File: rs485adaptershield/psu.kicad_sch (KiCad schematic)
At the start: 3 parts

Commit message: more work
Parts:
- added C10: 1u, Capacitor_SMD:C_1210_3225Metric, symbol Device:C
- added C11: 10p, Capacitor_SMD:C_1210_3225Metric, symbol Device:C
- added C7, C8: 22u, Capacitor_SMD:C_1210_3225Metric, symbol Device:C
- added C9: 100n, Capacitor_SMD:C_1210_3225Metric, symbol Device:C
- added R17: 47k, Resistor_SMD:R_0805_2012Metric, symbol Device:R
- added R18: 10k, Resistor_SMD:R_0805_2012Metric, symbol Device:R
- added U5: TPSM33606S5QRDNRQ1, RDN0011A_TEX, symbol TPSM33606S5QRDNRQ1:TPSM33606S5QRDNRQ1
- C3: value 22u -> 4.7u
- R10: value 470 -> 560
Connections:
- net GND: now also C10.2, C7.2, C8.2, C9.2, R18.2, U5.10 (GND), U5.11 (MODE/SYNCH)
- net +12V renamed VIN
- net VIN: now also C9.1, U5.2 (EN), U5.3 (VIN)
- net +5V renamed VUSB
- net VUSB: now also C11.1, C7.1, C8.1, R17.1, U5.4 (VOUT)
- new net: C10.1, U5.8 (VCC)
- new net FB: C11.2, R17.2, R18.1, U5.9 (FB)
- no-connect marks 0 -> 4
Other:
- moved on the sheet: C3

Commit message: more progress
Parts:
- removed D4: LED, LED_SMD:LED_0805_2012Metric, symbol Device:LED
- removed R10: 560, Resistor_SMD:R_0805_2012Metric, symbol Device:R
- added C13: 100n, Capacitor_SMD:C_1210_3225Metric, symbol Device:C
- added C14, C15: 22u, Capacitor_SMD:C_1210_3225Metric, symbol Device:C
- added C16: 1u, Capacitor_SMD:C_1210_3225Metric, symbol Device:C
- added C17: 10p, Capacitor_SMD:C_1210_3225Metric, symbol Device:C
- added C34: 100n, Capacitor_SMD:C_0603_1608Metric, symbol Device:C
- added C5: 4.7u, Capacitor_SMD:C_1210_3225Metric, symbol Device:C
- added R24: 50k, Resistor_SMD:R_0805_2012Metric, symbol Device:R
- added R25: 12k, Resistor_SMD:R_0805_2012Metric, symbol Device:R
- added R32: 330k, Capacitor_SMD:C_0402_1005Metric, symbol Device:R
- added U10: TPSM33606S5QRDNRQ1, RDN0011A_TEX, symbol TPSM33606S5QRDNRQ1:TPSM33606S5QRDNRQ1
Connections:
- net GND: now also C13.2, C14.2, C15.2, C16.2, C34.1, C5.2, R25.2, U10.10 (GND), U10.11 (MODE/SYNCH)
- net FB renamed FB1
- net VIN renamed VBATT
- net VBATT: now also C13.1, C5.1, R32.1, U10.3 (VIN); no longer U5.2 (EN)
- net VUSB renamed VUSB1
- net VUSB1: no longer C11.1, R17.1
- new net: C16.1, U10.8 (VCC)
- new net EN: C34.2, R32.2, U10.2 (EN), U5.2 (EN)
- new net FB2: C17.2, R24.2, R25.1, U10.9 (FB)
- new net VUSB2: C11.1, C14.1, C15.1, C17.1, R17.1, R24.1, U10.4 (VOUT)
- no-connect marks 4 -> 8
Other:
- note added: "make this switchable between 5v and 5.5V"
- note added: "testpads everywhere"
- moved on the sheet: C10, C11, C3, C7, C8, C9, R17, R18, U5

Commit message: schematic mostly finished w/o footprints
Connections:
- net VUSB1: now also C17.1, R24.1
- net VUSB2: no longer C17.1, R24.1
- net EN renamed USB_PSU_EN
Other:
- moved on the sheet: C13, C14, C15, C3, C5, C7, C8, C9

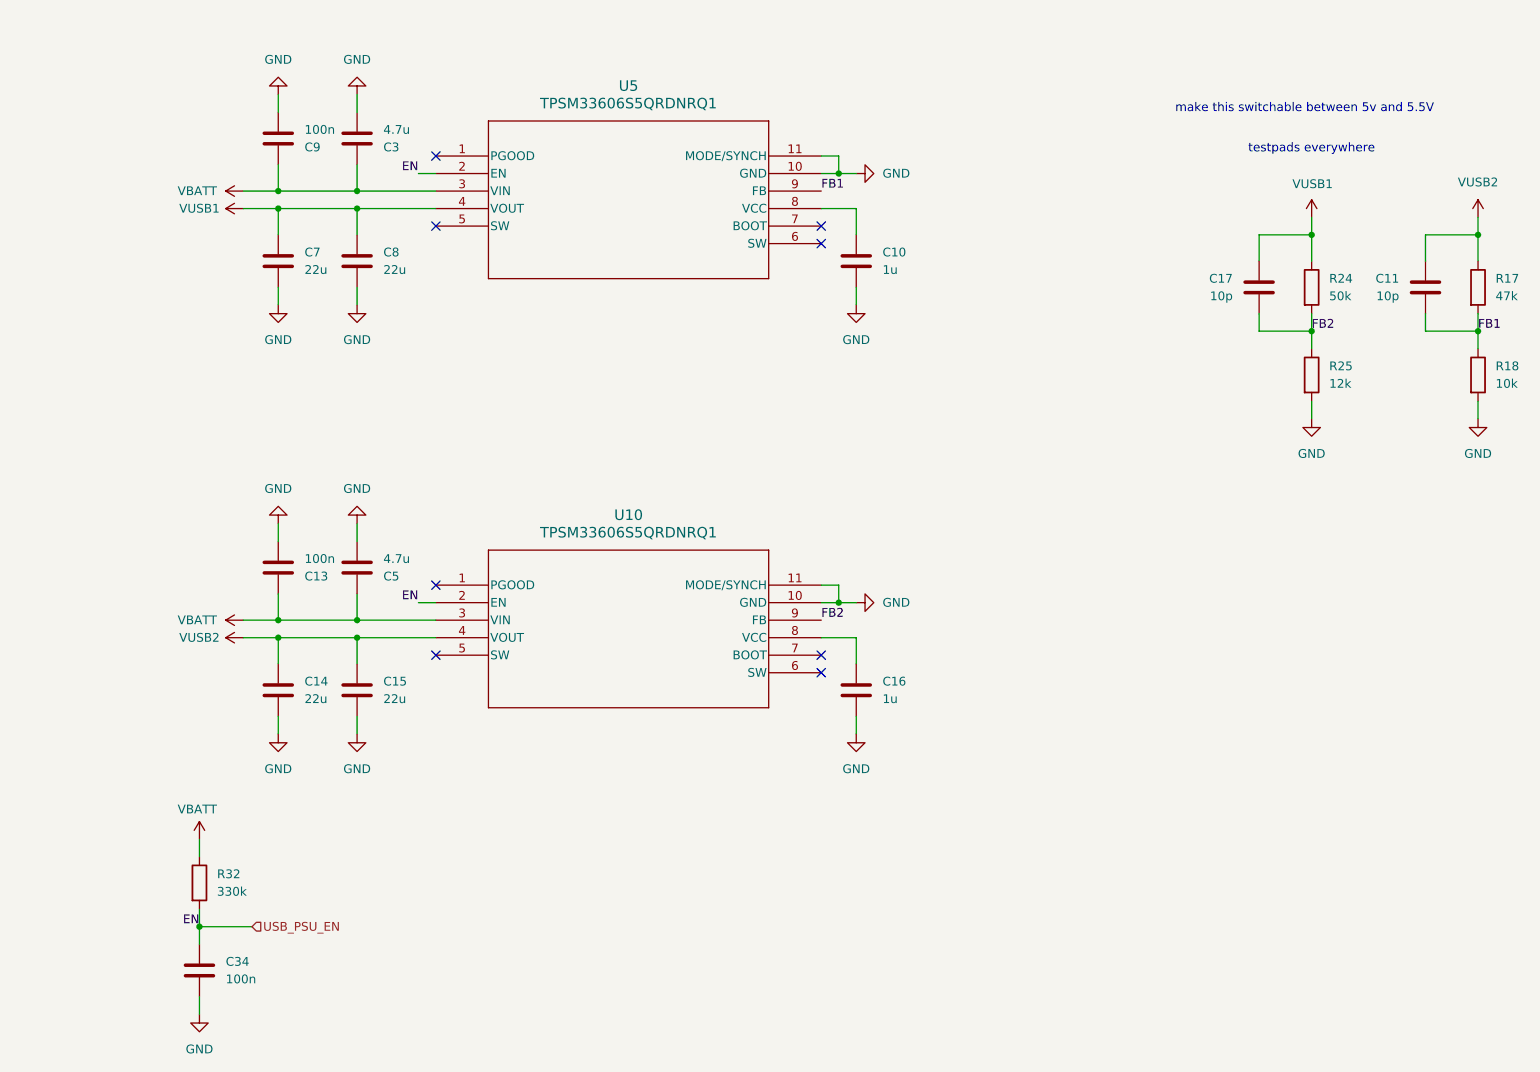
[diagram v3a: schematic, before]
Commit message: usb stackup problems
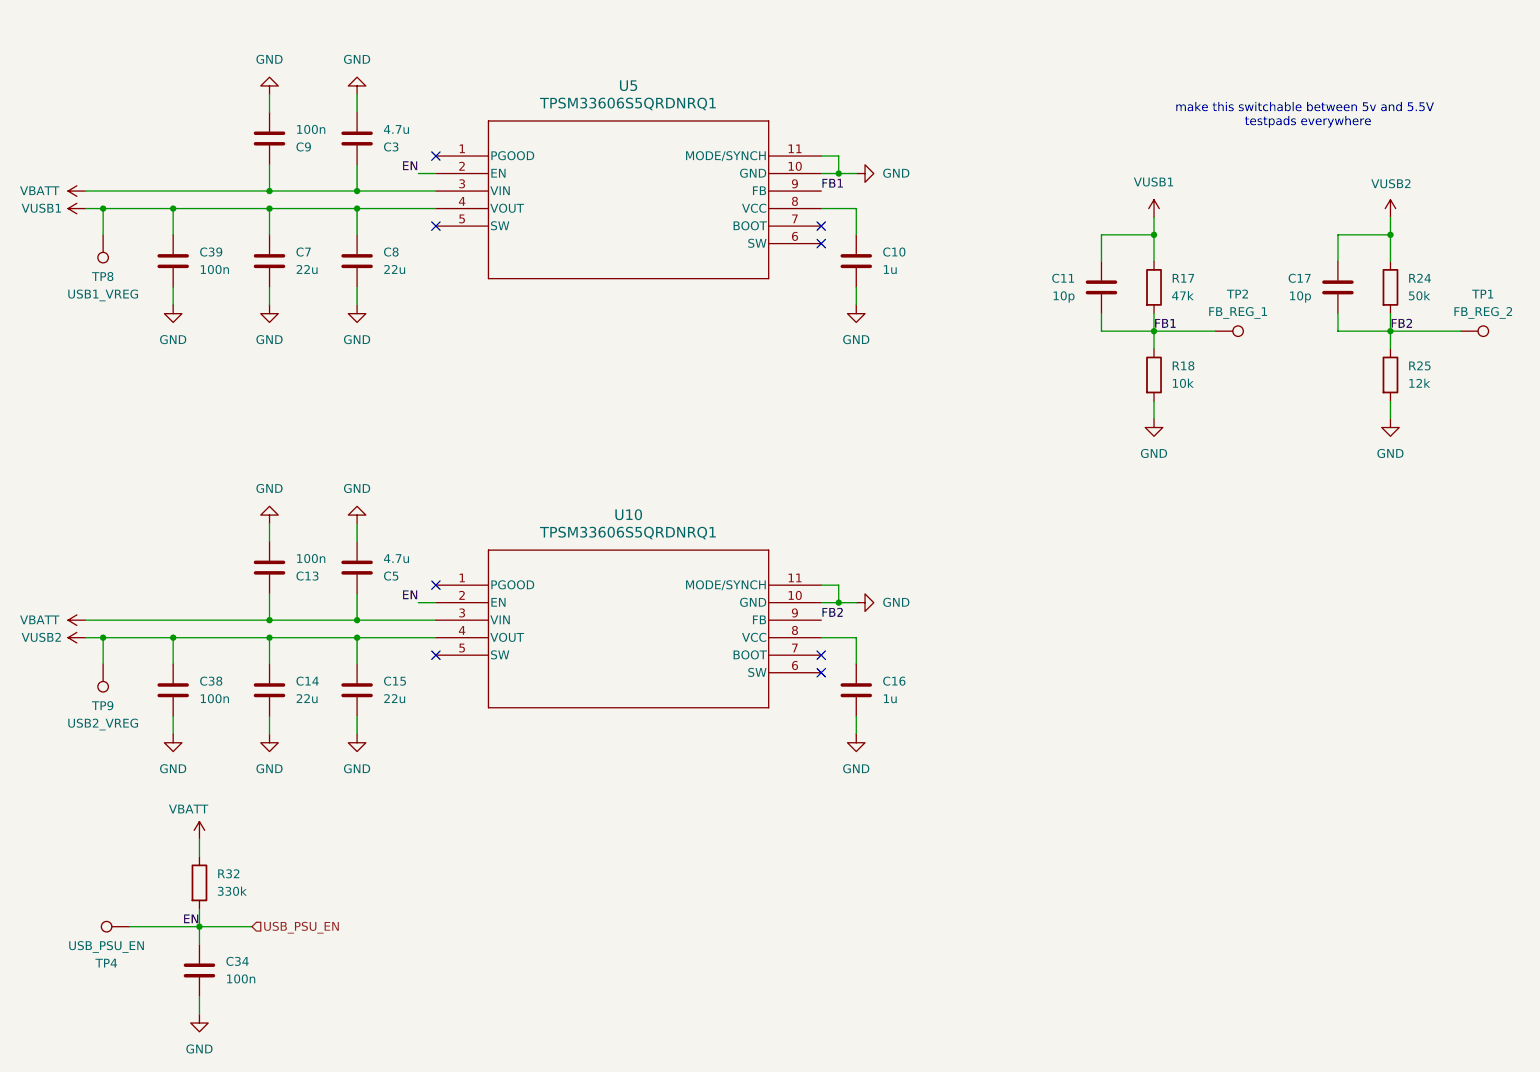
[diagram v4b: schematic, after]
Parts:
- added C38, C39: 100n, Capacitor_SMD:C_0402_1005Metric, symbol Device:C
- added TP1: FB_REG_2, TestPoint:TestPoint_Pad_D1.0mm, symbol Connector:TestPoint
- added TP2: FB_REG_1, TestPoint:TestPoint_Pad_D1.0mm, symbol Connector:TestPoint
- added TP4: USB_PSU_EN, TestPoint:TestPoint_Pad_D1.0mm, symbol Connector:TestPoint
- added TP8: USB1_VREG, TestPoint:TestPoint_Pad_D1.0mm, symbol Connector:TestPoint
- added TP9: USB2_VREG, TestPoint:TestPoint_Pad_D1.0mm, symbol Connector:TestPoint
- C10, C16: footprint Capacitor_SMD:C_1210_3225Metric -> Capacitor_SMD:C_0603_1608Metric
- C11, C13, C17, C9: footprint Capacitor_SMD:C_1210_3225Metric -> Capacitor_SMD:C_0402_1005Metric
- C3, C5: footprint Capacitor_SMD:C_1210_3225Metric -> Capacitor_SMD:C_0805_2012Metric
- C34: footprint Capacitor_SMD:C_0603_1608Metric -> Capacitor_SMD:C_0402_1005Metric
- R17, R18, R24, R25: footprint Resistor_SMD:R_0805_2012Metric -> Resistor_SMD:R_0402_1005Metric
- R32: footprint Capacitor_SMD:C_0402_1005Metric -> Resistor_SMD:R_0402_1005Metric
- U10, U5: footprint RDN0011A_TEX -> IMPORTED:RDN0011A_TEX
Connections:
- net FB1: now also TP2.1
- net FB2: now also TP1.1
- net GND: now also C38.2, C39.2
- net USB_PSU_EN: now also TP4.1
- net VUSB1: now also C11.1, R17.1, C39.1, TP8.1; no longer C17.1, R24.1
- net VUSB2: now also C17.1, R24.1, C38.1, TP9.1; no longer C11.1, R17.1
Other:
- moved on the sheet: C11, C13, C14, C17, C7, C9, R17, R18, R24, R25

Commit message: more layout
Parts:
- U10, U5: footprint IMPORTED:RDN0011A_TEX -> IMPORTED:RDN0011A_TEX_NEW
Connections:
- net VUSB1 renamed VUSB_B
- net VUSB2 renamed VUSB_A
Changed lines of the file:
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@@
 			)
 		)
-		(property "Value" "VUSB1"
+		(property "Value" "VUSB_B"
 			(at 20.32 71.12 90)
 			(show_name no)
@@
 		(in_pos_files yes)
 		(dnp no)
-		(fields_autoplaced yes)
 		(property "Reference" "#PWR063"
 			(at 181.61 76.2 0)
@@
 			)
 		)
-		(property "Value" "VUSB1"
-			(at 181.61 67.31 0)
+		(property "Value" "VUSB_B"
+			(at 178.562 67.818 0)
 			(show_name no)
 			(do_not_autoplace no)
@@
 					(size 1.27 1.27)
 				)
+				(justify left)
 			)
 		)
@@
 			)
 		)
-		(property "Footprint" "IMPORTED:RDN0011A_TEX"
+		(property "Footprint" "IMPORTED:RDN0011A_TEX_NEW"
 			(at 77.47 63.5 0)
 			(hide yes)
@@
 			)
 		)
-		(property "Value" "VUSB2"
+		(property "Value" "VUSB_A"
 			(at 20.32 133.35 90)
 			(show_name no)
@@
 			)
 		)
-		(property "Footprint" "IMPORTED:RDN0011A_TEX"
+		(property "Footprint" "IMPORTED:RDN0011A_TEX_NEW"
 			(at 77.47 125.73 0)
 			(hide yes)
@@
 			)
 		)
-		(property "Value" "VUSB2"
-			(at 213.106 67.564 0)
+		(property "Value" "VUSB_A"
+			(at 212.344 67.564 0)
 			(show_name no)
 			(do_not_autoplace no)
